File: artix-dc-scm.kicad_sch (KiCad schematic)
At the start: 4 parts

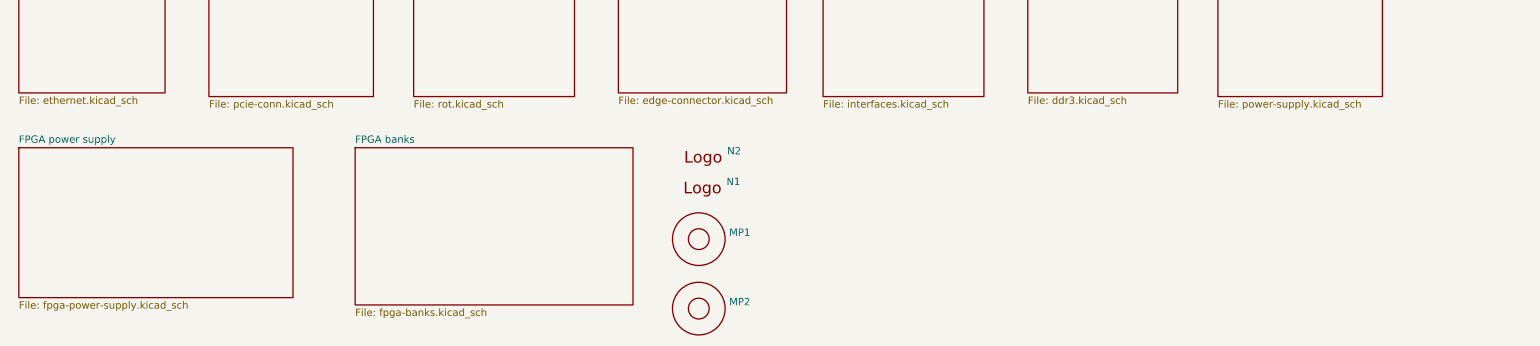
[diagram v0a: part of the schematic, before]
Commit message: Introduce component standardization
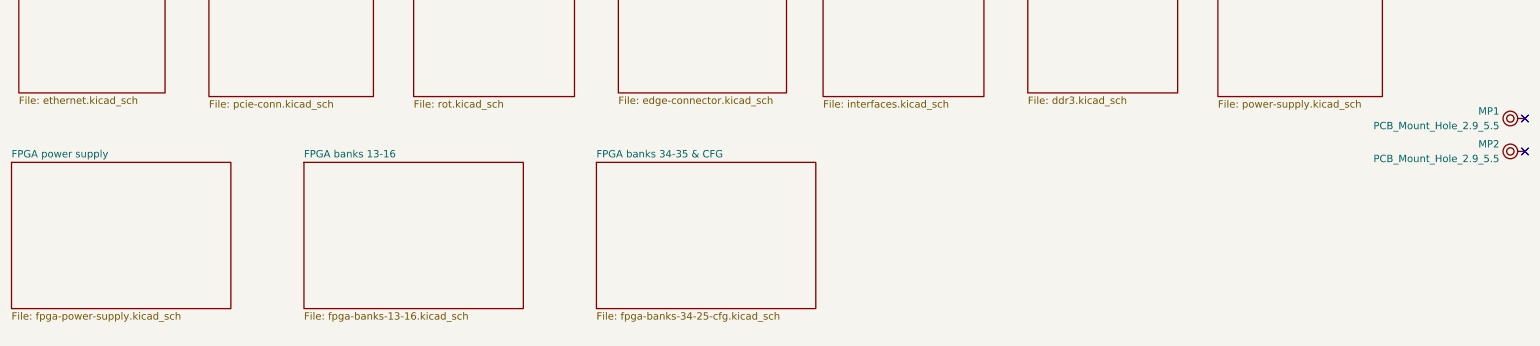
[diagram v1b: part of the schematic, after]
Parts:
- removed N1: (no value), symbol artix-dc-scm:antmicro_logo
- removed N2: (no value), symbol artix-dc-scm:oshw_logo
- MP1, MP2: value (none) -> PCB_Mount_Hole_2.9_5.5; footprint (none) -> antmicro-footprints:mounting-hole-2.9mm-5.5mm; symbol artix-dc-scm:PCB_Mount_Hole_2.9_5.5 -> antmicroMechanicalParts:PCB_Mount_Hole_2.9_5.5; Author (none) -> Antmicro; DNP (none) -> DNP; License (none) -> Apache-2.0
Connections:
- no-connect marks 0 -> 2
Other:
- sheet FPGA banks renamed FPGA banks 13-16
- added sheet FPGA banks 34-35 & CFG (fpga-banks-34-25-cfg.kicad_sch)
- sheet FPGA banks 13-16: file fpga-banks.kicad_sch -> fpga-banks-13-16.kicad_sch
